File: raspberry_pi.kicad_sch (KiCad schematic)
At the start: 6 parts, among them J29 Raspberry_Pi_2_3, Q7 DMMT5401, Q8 DMG2305UX

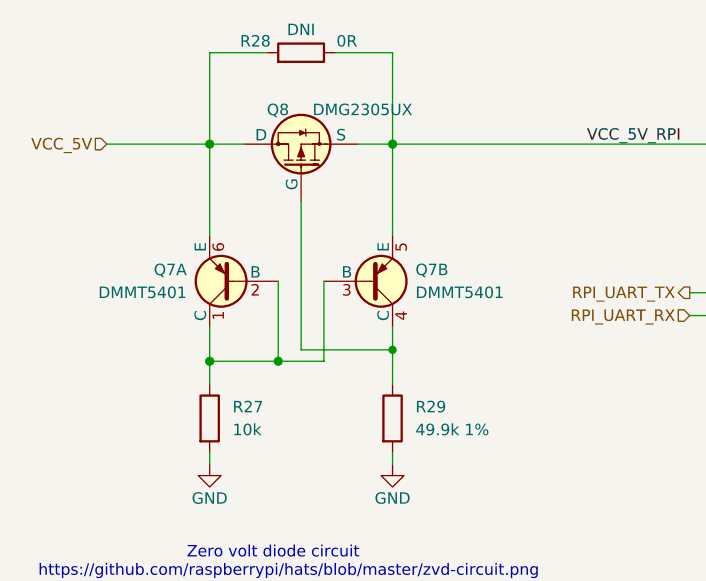
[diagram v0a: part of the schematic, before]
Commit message: Refactored top sheet
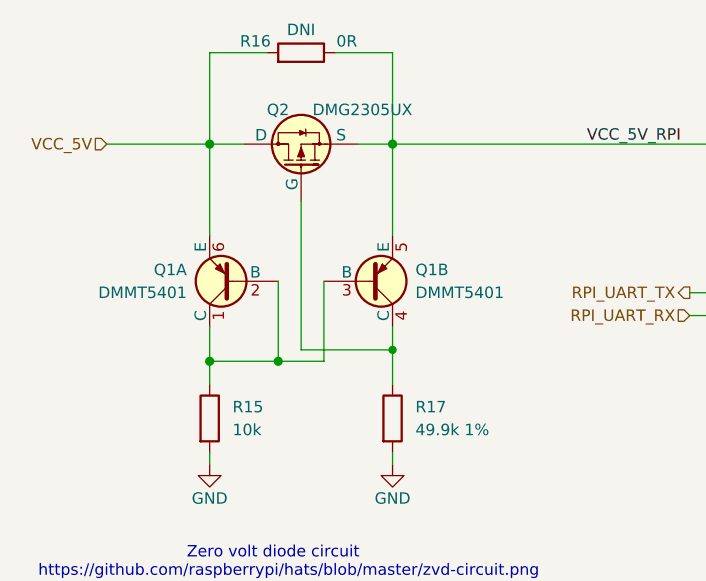
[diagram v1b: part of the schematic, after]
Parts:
- renumbered Q7 to Q1, Q8 to Q2, R27 to R15, R28 to R16, R29 to R17
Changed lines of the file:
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@@
   (symbol (lib_id "raspberrypi_hat:DMG2305UX") (at 59.69 35.56 90) (unit 1)
     (in_bom yes) (on_board yes)
-    (property "Reference" "Q8" (id 0) (at 55.88 31.75 90)
+    (property "Reference" "Q2" (id 0) (at 55.88 31.75 90)
       (effects (font (size 1.27 1.27)) (justify right))
     )
@@
   (symbol (lib_id "PersonnalSymbolLibrary:DMMT5401") (at 52.07 50.8 180) (unit 1)
     (in_bom yes) (on_board yes) (fields_autoplaced)
-    (property "Reference" "Q7" (id 0) (at 46.99 49.5299 0)
+    (property "Reference" "Q1" (id 0) (at 46.99 49.5299 0)
       (effects (font (size 1.27 1.27)) (justify left))
     )
@@
   (symbol (lib_id "Device:R") (at 59.69 25.4 270) (mirror x) (unit 1)
     (in_bom yes) (on_board yes)
-    (property "Reference" "R28" (id 0) (at 54.61 24.13 90))
+    (property "Reference" "R16" (id 0) (at 54.61 24.13 90))
     (property "Value" "0R" (id 1) (at 64.77 24.13 90))
     (property "Footprint" "Resistor_SMD:R_0805_2012Metric" (id 2) (at 59.69 27.178 90)
@@
   (symbol (lib_id "PersonnalSymbolLibrary:DMMT5401") (at 67.31 50.8 0) (mirror x) (unit 2)
     (in_bom yes) (on_board yes) (fields_autoplaced)
-    (property "Reference" "Q7" (id 0) (at 72.39 49.5299 0)
+    (property "Reference" "Q1" (id 0) (at 72.39 49.5299 0)
       (effects (font (size 1.27 1.27)) (justify left))
     )
@@
   (symbol (lib_id "Device:R") (at 49.53 66.04 0) (unit 1)
     (in_bom yes) (on_board yes) (fields_autoplaced)
-    (property "Reference" "R27" (id 0) (at 52.07 64.7699 0)
+    (property "Reference" "R15" (id 0) (at 52.07 64.7699 0)
       (effects (font (size 1.27 1.27)) (justify left))
     )
@@
   (symbol (lib_id "Device:R") (at 69.85 66.04 0) (unit 1)
     (in_bom yes) (on_board yes)
-    (property "Reference" "R29" (id 0) (at 72.39 64.7699 0)
+    (property "Reference" "R17" (id 0) (at 72.39 64.7699 0)
       (effects (font (size 1.27 1.27)) (justify left))
     )
@@
   (symbol (lib_id "power:GND") (at 49.53 71.12 0) (unit 1)
     (in_bom yes) (on_board yes)
-    (property "Reference" "#PWR075" (id 0) (at 49.53 77.47 0)
+    (property "Reference" "#PWR061" (id 0) (at 49.53 77.47 0)
       (effects (font (size 1.27 1.27)) hide)
     )
@@
   (symbol (lib_id "power:GND") (at 69.85 71.12 0) (unit 1)
     (in_bom yes) (on_board yes)
-    (property "Reference" "#PWR076" (id 0) (at 69.85 77.47 0)
+    (property "Reference" "#PWR062" (id 0) (at 69.85 77.47 0)
       (effects (font (size 1.27 1.27)) hide)
     )
